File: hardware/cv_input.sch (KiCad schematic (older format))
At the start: 12 parts

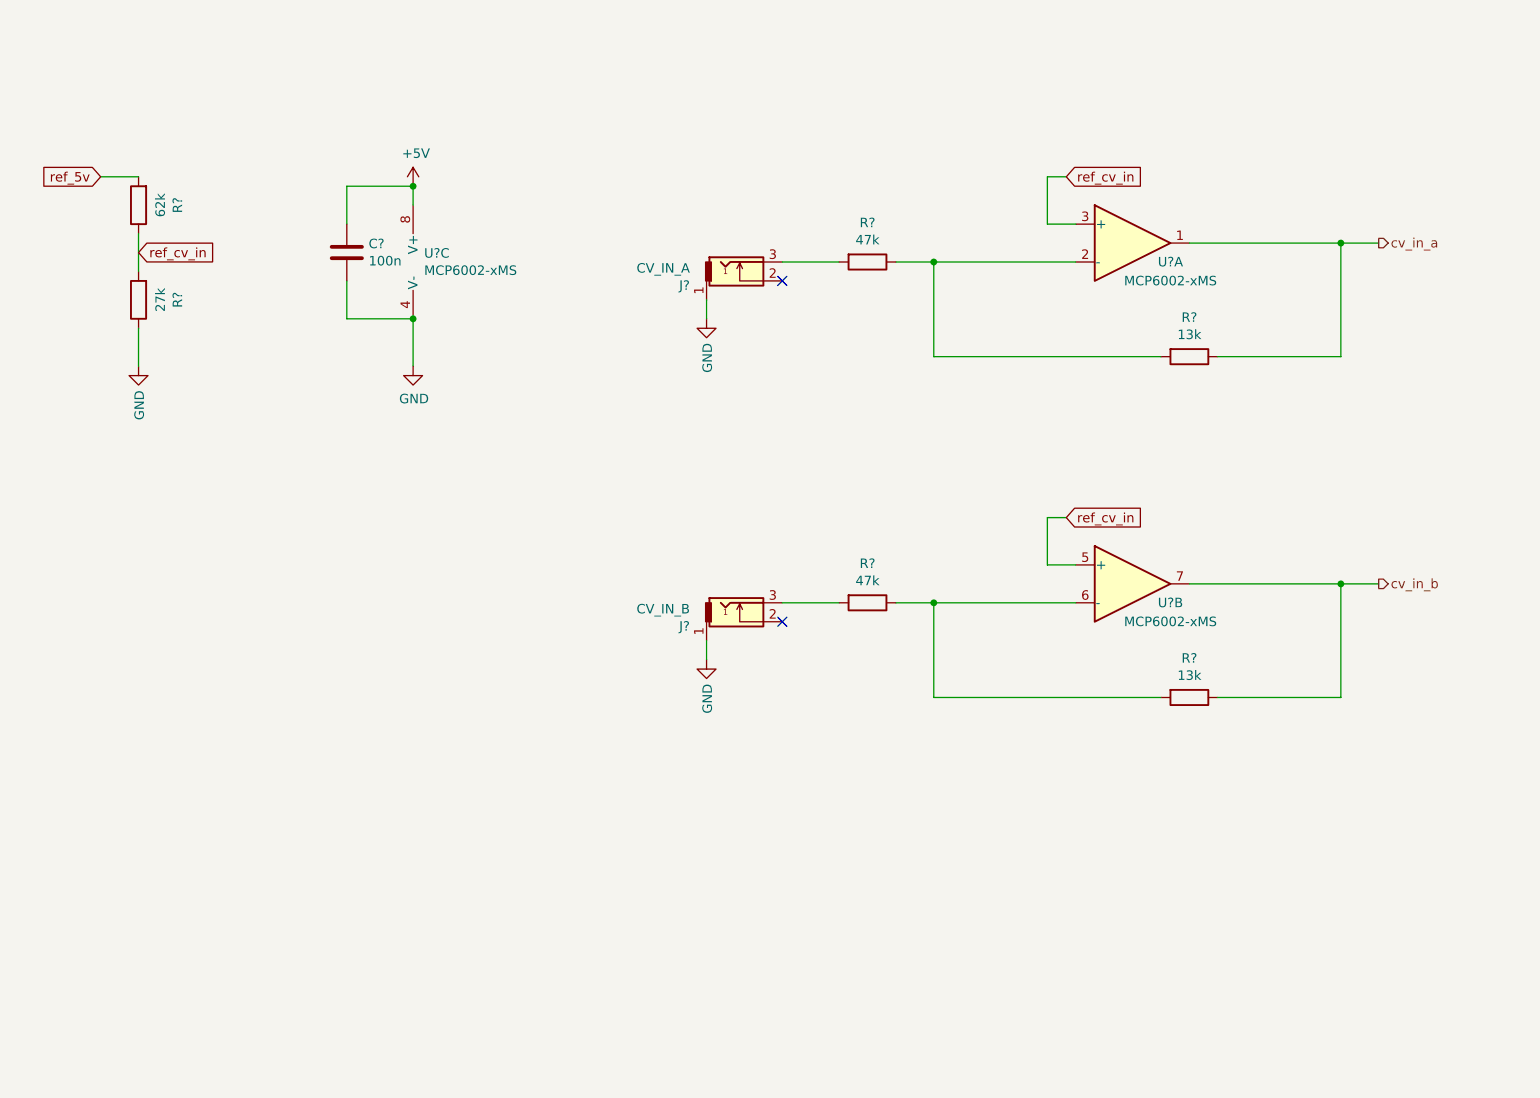
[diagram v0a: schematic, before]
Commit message: Adjust CV-ins
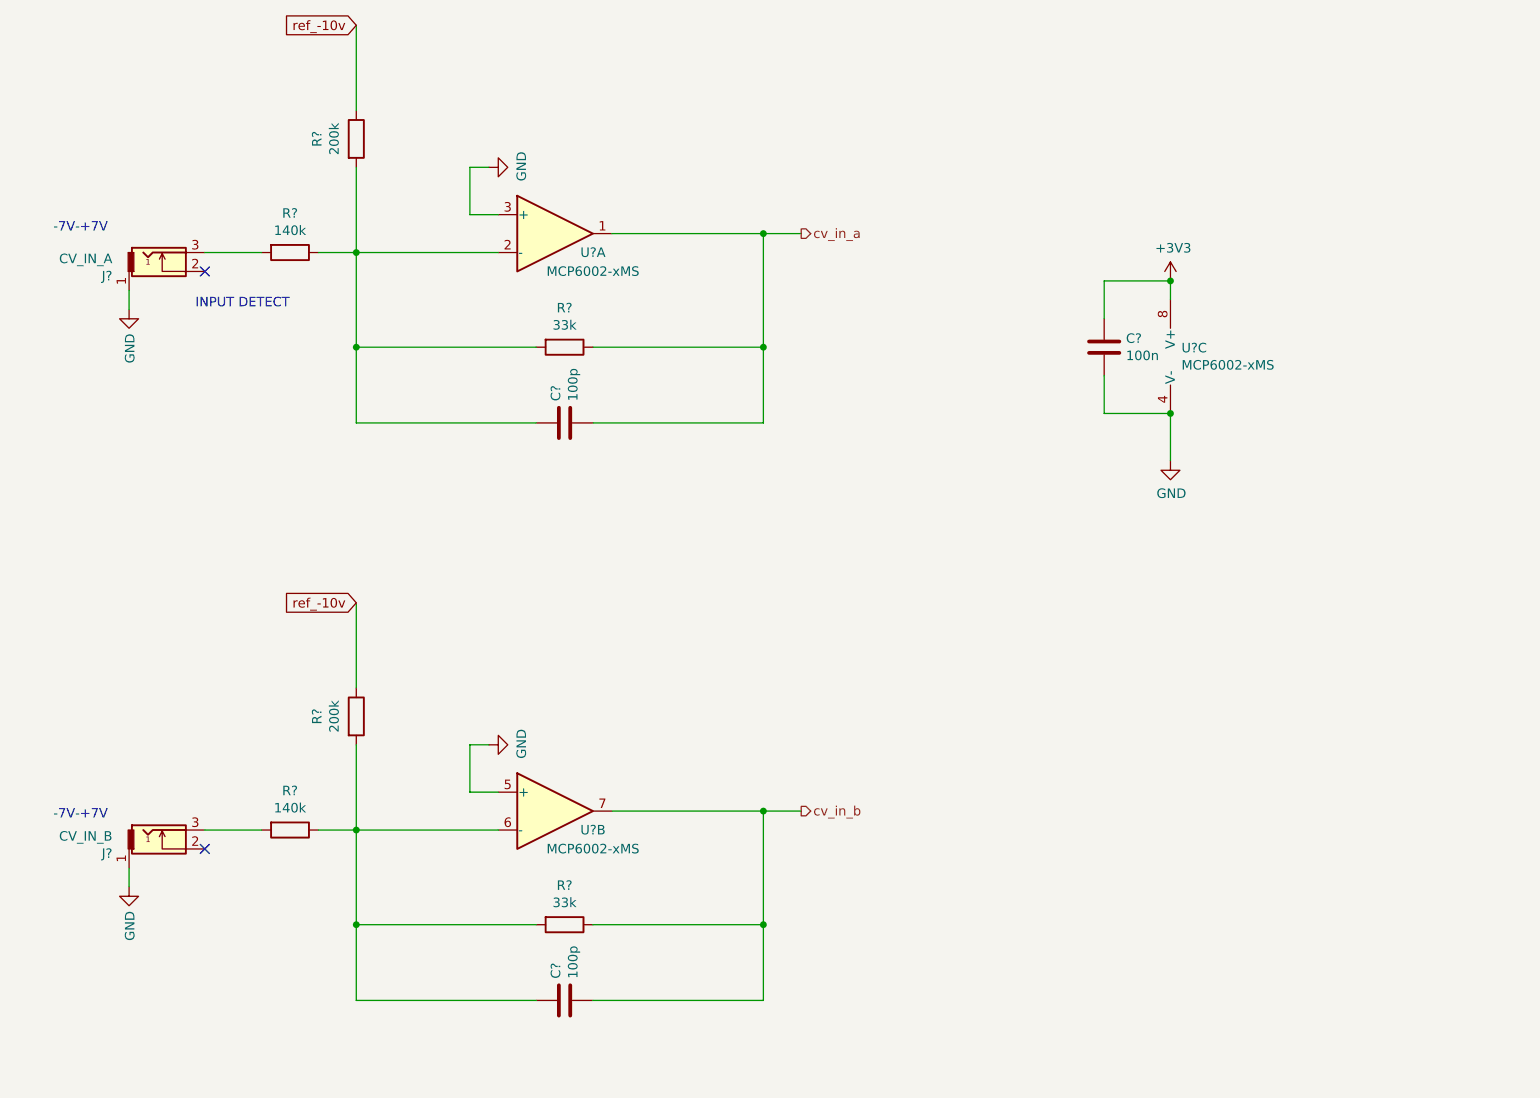
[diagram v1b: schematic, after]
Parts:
- removed R?: 62k, symbol Device:R
- removed R?: 27k, symbol Device:R
- added C? (x2): 100p, symbol Device:C
- added R? (x2): 200k, symbol Device:R
- R? (x2): value 13k -> 33k
- R? (x2): value 47k -> 140k
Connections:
- net ref_cv_in is gone; now on net GND: U?.3 (+), U?.5 (+)
- net cv_in_a: now also C?.2
- net cv_in_b: now also C?.2
- net at R?.1, R?.2, U?.2 (-): now also C?.1, R?.2
- net at R?.1, R?.2, U?.6 (-): now also C?.1, R?.2
- net +5V renamed +3V3
- new net ref_-10v: R?.1, R?.1
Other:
- note added: "-7V-+7V"
- note added: "INPUT DETECT"
- moved on the sheet: C?, J?, R?, U?A, U?B, U?C

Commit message: Add more schematics:
- Faders
- Step LEDs
- Trigger output
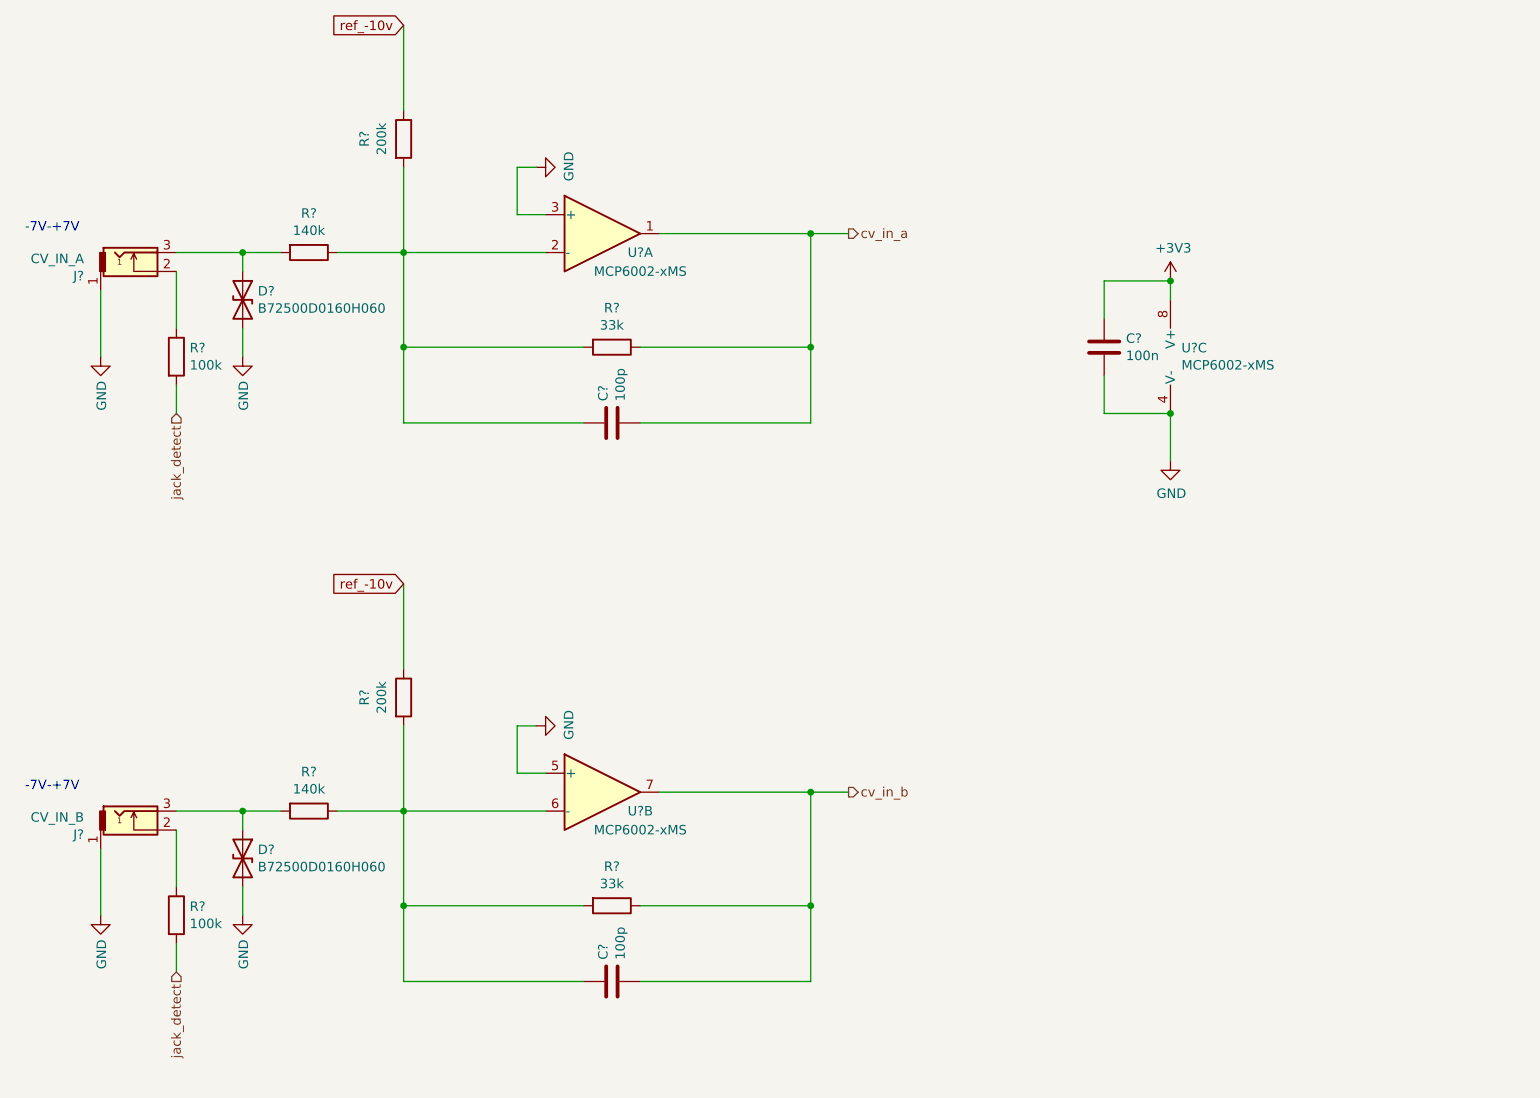
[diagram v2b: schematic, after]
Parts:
- removed C?: 100p, symbol Device:C
- removed J?: CV_IN_B, symbol thonkiconn_jackSocket_fuzzySi:fuzzySI_thonkiconn
- removed R?: 33k, symbol Device:R
- removed R?: 140k, symbol Device:R
- removed R?: 200k, symbol Device:R
- removed U?: MCP6002-xMS, symbol Amplifier_Operational:MCP6002-xMS
- added C?: 100p, symbol Device:C
- added D? (x2): B72500D0160H060, Diode_SMD:D_0603_1608Metric, symbol Device:D_TVS
- added J?: CV_IN_B, symbol thonkiconn_jackSocket_fuzzySi:fuzzySI_thonkiconn
- added R? (x2): 100k, symbol Device:R
- added R?: 33k, symbol Device:R
- added R?: 140k, symbol Device:R
- added R?: 200k, symbol Device:R
- added U?: MCP6002-xMS, symbol Amplifier_Operational:MCP6002-xMS
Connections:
- net GND: now also D?.2 (A2), D?.2 (A2), J?.1, U?.5 (+)
- net cv_in_b: now also C?.2, R?.1, U?.7
- net ref_-10v: now also R?.1
- net at J?.3, R?.2: now also D?.1 (A1)
- net at J?.2: now also R?.1
- new net: J?.2, R?.1
- new net: C?.1, R?.1, R?.2, R?.2, U?.6 (-)
- new net: D?.1 (A1), J?.3, R?.2
- new net jack_detect: R?.2, R?.2
- no-connect marks 2 -> 0
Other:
- note removed: "INPUT DETECT"
- moved on the sheet: C?, J?, R?, U?A

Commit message: Minor adjustments to schematics before PCB
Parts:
- removed J?: CV_IN_A, symbol thonkiconn_jackSocket_fuzzySi:fuzzySI_thonkiconn
- removed J?: CV_IN_B, symbol thonkiconn_jackSocket_fuzzySi:fuzzySI_thonkiconn
- added J10, J9: PJ398SM, Connector_Audio:Jack_3.5mm_QingPu_WQP-PJ398SM_Vertical_CircularHoles, symbol Connector:AudioJack2_SwitchT
- added R37, R38: 100R, Resistor_SMD:R_0603_1608Metric, symbol Device:R
- C41, C42, C43: renamed from C?; footprint (none) -> Capacitor_SMD:C_0603_1608Metric
- R29, R30, R31, R32, R33, R34, R35, R36: renamed from R?; footprint (none) -> Resistor_SMD:R_0603_1608Metric
- U6: renamed from U?; footprint (none) -> Package_SO:SOIC-8_3.9x4.9mm_P1.27mm
- gave numbers to parts that had none: 2
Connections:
- net GND: now also J10.S, J9.S
- net cv_in_a: now also R37.1; no longer C41.2, R35.1, U6.1
- net cv_in_b: now also R38.1; no longer C42.2, R36.1, U6.7
- net at D12.1 (A1), R31.2: now also J9.T
- net at R29.1: now also J9.TN
- net at R30.1: now also J10.TN
- net at D13.1 (A1), R32.2: now also J10.T
- new net: C41.2, R35.1, R37.2, U6.1
- new net: C42.2, R36.1, R38.2, U6.7
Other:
- moved on the sheet: C41, C42, C43, R35, R36, U6C

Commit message: Last adjustments to hardware before v0.1 release
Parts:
- C43: renamed from C41; LCSC (none) -> C14858; LCSC Part # (none) -> C14858
- C44: renamed from C42; LCSC (none) -> C14858; LCSC Part # (none) -> C14858
- C45: renamed from C43; LCSC (none) -> C14663; LCSC Part # (none) -> C14663
- R29, R30: LCSC (none) -> C25803; LCSC Part # (none) -> C25803
- R33, R34: LCSC (none) -> C25811; LCSC Part # (none) -> C25811
- R35, R36: LCSC (none) -> C4216; LCSC Part # (none) -> C4216
- R37, R38: LCSC (none) -> C22775; LCSC Part # (none) -> C22775
- U6: LCSC (none) -> C7377; LCSC Part # (none) -> C7377
- renumbered D12 to D13, D13 to D14
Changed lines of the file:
@@
 F 2 "Package_SO:SOIC-8_3.9x4.9mm_P1.27mm" H 4400 2150 50  0001 C CNN
 F 3 "http://ww1.microchip.com/downloads/en/DeviceDoc/21733j.pdf" H 4400 2150 50  0001 C CNN
+F 4 "C7377" H 4400 2150 50  0001 C CNN "LCSC Part #"
+F 5 "C7377" H 4400 2150 50  0001 C CNN "LCSC"
 	1    4400 2150
 	1    0    0    -1
@@
 F 2 "Package_SO:SOIC-8_3.9x4.9mm_P1.27mm" H 8700 2500 50  0001 C CNN
 F 3 "http://ww1.microchip.com/downloads/en/DeviceDoc/21733j.pdf" H 8700 2500 50  0001 C CNN
+F 4 "C7377" H 8700 2500 50  0001 C CNN "LCSC Part #"
+F 5 "C7377" H 8700 2500 50  0001 C CNN "LCSC"
 	3    8700 2500
 	1    0    0    -1
 $EndComp
 $Comp
-L power:GND #PWR0113
+L power:GND #PWR0120
 U 1 1 5FCC637B
 P 8600 3050
-F 0 "#PWR0113" H 8600 2800 50  0001 C CNN
+F 0 "#PWR0120" H 8600 2800 50  0001 C CNN
 F 1 "GND" H 8605 2877 50  0000 C CNN
 F 2 "" H 8600 3050 50  0001 C CNN
@@
 $EndComp
 $Comp
-L Device:C C43
+L Device:C C45
 U 1 1 5FCCAC86
 P 8250 2450
-F 0 "C43" H 8365 2496 50  0000 L CNN
+F 0 "C45" H 8365 2496 50  0000 L CNN
 F 1 "100n" H 8365 2405 50  0000 L CNN
 F 2 "Capacitor_SMD:C_0603_1608Metric" H 8288 2300 50  0001 C CNN
 F 3 "~" H 8250 2450 50  0001 C CNN
+F 4 "C14663" H 8250 2450 50  0001 C CNN "LCSC Part #"
+F 5 "C14663" H 8250 2450 50  0001 C CNN "LCSC"
 	1    8250 2450
 	1    0    0    -1
@@
 F 2 "Resistor_SMD:R_0603_1608Metric" V 4130 2750 50  0001 C CNN
 F 3 "~" H 4200 2750 50  0001 C CNN
+F 4 "C4216" H 4200 2750 50  0001 C CNN "LCSC Part #"
+F 5 "C4216" H 4200 2750 50  0001 C CNN "LCSC"
 	1    4200 2750
 	0    1    1    0
@@
 ref_-10v
 $Comp
-L power:GND #PWR0110
+L power:GND #PWR0117
 U 1 1 5FD46DBF
 P 4050 1800
-F 0 "#PWR0110" H 4050 1550 50  0001 C CNN
+F 0 "#PWR0117" H 4050 1550 50  0001 C CNN
 F 1 "GND" H 4055 1627 50  0000 C CNN
 F 2 "" H 4050 1800 50  0001 C CNN
@@
 Connection ~ 3350 2750
 $Comp
-L Device:C C41
+L Device:C C43
 U 1 1 5FD4B56E
 P 4200 3150
-F 0 "C41" H 4315 3196 50  0000 L CNN
+F 0 "C43" H 4315 3196 50  0000 L CNN
 F 1 "100p" H 4315 3105 50  0000 L CNN
 F 2 "Capacitor_SMD:C_0603_1608Metric" H 4238 3000 50  0001 C CNN
 F 3 "~" H 4200 3150 50  0001 C CNN
+F 4 "C14858" H 4200 3150 50  0001 C CNN "LCSC Part #"
+F 5 "C14858" H 4200 3150 50  0001 C CNN "LCSC"
 	1    4200 3150
 	0    -1   -1   0
@@
 F 2 "Resistor_SMD:R_0603_1608Metric" V 3280 1650 50  0001 C CNN
 F 3 "~" H 3350 1650 50  0001 C CNN
+F 4 "C25811" H 3350 1650 50  0001 C CNN "LCSC Part #"
+F 5 "C25811" H 3350 1650 50  0001 C CNN "LCSC"
 	1    3350 1650
 	1    0    0    -1
@@
 	3350 1800 3350 2250
 $Comp
-L power:+3V3 #PWR0112
+L power:+3V3 #PWR0119
 U 1 1 5FDAD355
 P 8600 2100
-F 0 "#PWR0112" H 8600 1950 50  0001 C CNN
+F 0 "#PWR0119" H 8600 1950 50  0001 C CNN
 F 1 "+3V3" H 8615 2273 50  0000 C CNN
 F 2 "" H 8600 2100 50  0001 C CNN
@@
 -7V-+7V
 $Comp
-L Device:D_TVS D12
+L Device:D_TVS D13
 U 1 1 5FE45F85
 P 2500 2500
-F 0 "D12" V 2454 2580 50  0000 L CNN
+F 0 "D13" V 2454 2580 50  0000 L CNN
 F 1 "B72500D0160H060" V 2545 2580 50  0000 L CNN
 F 2 "Diode_SMD:D_0603_1608Metric" H 2500 2500 50  0001 C CNN
@@
 P 2250 1850
 AR Path="/5ED37B53/5FB5AC07/5FCFECAE" Ref="#PWR?"  Part="1"
-AR Path="/5FCA3E21/5FCFECAE" Ref="#PWR0106"  Part="1"
-F 0 "#PWR0106" H 2250 1600 50  0001 C CNN
+AR Path="/5FCA3E21/5FCFECAE" Ref="#PWR0113"  Part="1"
+F 0 "#PWR0113" H 2250 1600 50  0001 C CNN
 F 1 "GND" V 2255 1722 50  0000 R CNN
 F 2 "" H 2250 1850 50  0001 C CNN
@@
 P 2500 2800
 AR Path="/5ED37B53/5FB5AC07/5FE4DBBE" Ref="#PWR?"  Part="1"
-AR Path="/5FCA3E21/5FE4DBBE" Ref="#PWR0108"  Part="1"
-F 0 "#PWR0108" H 2500 2550 50  0001 C CNN
+AR Path="/5FCA3E21/5FE4DBBE" Ref="#PWR0115"  Part="1"
+F 0 "#PWR0115" H 2500 2550 50  0001 C CNN
 F 1 "GND" V 2505 2672 50  0000 R CNN
 F 2 "" H 2500 2800 50  0001 C CNN
@@
 F 2 "Package_SO:SOIC-8_3.9x4.9mm_P1.27mm" H 4400 5100 50  0001 C CNN
 F 3 "http://ww1.microchip.com/downloads/en/DeviceDoc/21733j.pdf" H 4400 5100 50  0001 C CNN
+F 4 "C7377" H 4400 5100 50  0001 C CNN "LCSC Part #"
+F 5 "C7377" H 4400 5100 50  0001 C CNN "LCSC"
 	2    4400 5100
 	1    0    0    -1
@@
 F 2 "Resistor_SMD:R_0603_1608Metric" V 4130 5700 50  0001 C CNN
 F 3 "~" H 4200 5700 50  0001 C CNN
+F 4 "C4216" H 4200 5700 50  0001 C CNN "LCSC Part #"
+F 5 "C4216" H 4200 5700 50  0001 C CNN "LCSC"
 	1    4200 5700
 	0    1    1    0
@@
 ref_-10v
 $Comp
-L power:GND #PWR0111
+L power:GND #PWR0118
 U 1 1 5FE5D6C4
 P 4050 4750
-F 0 "#PWR0111" H 4050 4500 50  0001 C CNN
+F 0 "#PWR0118" H 4050 4500 50  0001 C CNN
 F 1 "GND" H 4055 4577 50  0000 C CNN
 F 2 "" H 4050 4750 50  0001 C CNN
@@
 Connection ~ 3350 5700
 $Comp
-L Device:C C42
+L Device:C C44
 U 1 1 5FE5D6CF
 P 4200 6100
-F 0 "C42" H 4315 6146 50  0000 L CNN
+F 0 "C44" H 4315 6146 50  0000 L CNN
 F 1 "100p" H 4315 6055 50  0000 L CNN
 F 2 "Capacitor_SMD:C_0603_1608Metric" H 4238 5950 50  0001 C CNN
 F 3 "~" H 4200 6100 50  0001 C CNN
+F 4 "C14858" H 4200 6100 50  0001 C CNN "LCSC Part #"
+F 5 "C14858" H 4200 6100 50  0001 C CNN "LCSC"
 	1    4200 6100
 	0    -1   -1   0
@@
 F 2 "Resistor_SMD:R_0603_1608Metric" V 3280 4600 50  0001 C CNN
 F 3 "~" H 3350 4600 50  0001 C CNN
+F 4 "C25811" H 3350 4600 50  0001 C CNN "LCSC Part #"
+F 5 "C25811" H 3350 4600 50  0001 C CNN "LCSC"
 	1    3350 4600
 	1    0    0    -1
@@
 -7V-+7V
 $Comp
-L Device:D_TVS D13
+L Device:D_TVS D14
 U 1 1 5FE5D6DF
 P 2500 5450
-F 0 "D13" V 2454 5530 50  0000 L CNN
+F 0 "D14" V 2454 5530 50  0000 L CNN
 F 1 "B72500D0160H060" V 2545 5530 50  0000 L CNN
 F 2 "Diode_SMD:D_0603_1608Metric" H 2500 5450 50  0001 C CNN
@@
 P 2500 5750
 AR Path="/5ED37B53/5FB5AC07/5FE5D6EE" Ref="#PWR?"  Part="1"
-AR Path="/5FCA3E21/5FE5D6EE" Ref="#PWR0109"  Part="1"
-F 0 "#PWR0109" H 2500 5500 50  0001 C CNN
+AR Path="/5FCA3E21/5FE5D6EE" Ref="#PWR0116"  Part="1"
+F 0 "#PWR0116" H 2500 5500 50  0001 C CNN
 F 1 "GND" V 2505 5622 50  0000 R CNN
 F 2 "" H 2500 5750 50  0001 C CNN
@@
 F 2 "Resistor_SMD:R_0603_1608Metric" V 2080 2800 50  0001 C CNN
 F 3 "~" H 2150 2800 50  0001 C CNN
+F 4 "C25803" H 2150 2800 50  0001 C CNN "LCSC Part #"
+F 5 "C25803" H 2150 2800 50  0001 C CNN "LCSC"
 	1    2150 2800
 	1    0    0    -1
@@
 F 2 "Resistor_SMD:R_0603_1608Metric" V 2080 5750 50  0001 C CNN
 F 3 "~" H 2150 5750 50  0001 C CNN
+F 4 "C25803" H 2150 5750 50  0001 C CNN "LCSC Part #"
+F 5 "C25803" H 2150 5750 50  0001 C CNN "LCSC"
 	1    2150 5750
 	1    0    0    -1
@@
 F 2 "Resistor_SMD:R_0603_1608Metric" V 5280 2150 50  0001 C CNN
 F 3 "~" H 5350 2150 50  0001 C CNN
+F 4 "C22775" H 5350 2150 50  0001 C CNN "LCSC Part #"
+F 5 "C22775" H 5350 2150 50  0001 C CNN "LCSC"
 	1    5350 2150
 	0    1    1    0
@@
 F 2 "Resistor_SMD:R_0603_1608Metric" V 5280 5100 50  0001 C CNN
 F 3 "~" H 5350 5100 50  0001 C CNN
+F 4 "C22775" H 5350 5100 50  0001 C CNN "LCSC Part #"
+F 5 "C22775" H 5350 5100 50  0001 C CNN "LCSC"
 	1    5350 5100
 	0    1    1    0
@@
 P 2250 4800
 AR Path="/5ED37B53/5FB5AC07/5FEE2B4E" Ref="#PWR?"  Part="1"
-AR Path="/5FCA3E21/5FEE2B4E" Ref="#PWR0107"  Part="1"
-F 0 "#PWR0107" H 2250 4550 50  0001 C CNN
+AR Path="/5FCA3E21/5FEE2B4E" Ref="#PWR0114"  Part="1"
+F 0 "#PWR0114" H 2250 4550 50  0001 C CNN
 F 1 "GND" V 2255 4672 50  0000 R CNN
 F 2 "" H 2250 4800 50  0001 C CNN
